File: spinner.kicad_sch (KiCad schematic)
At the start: 131 parts, among them J1 Micro_SD_Card, J301 USB_C_Receptacle_USB2.0_16P, J302 Conn_01x02_Pin, SW1 SW_SPDT, U2 RS0102, U301 BQ24073RGT, U302 SPX3819M5-L-3-3, U303 TPS61022, u10 ESP32-S3-WROOM-1

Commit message: Added a few more pinouts to the CPU.
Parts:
- added C301: 1uF, Capacitor_SMD:C_0805_2012Metric_Pad1.18x1.45mm_HandSolder, symbol Device:C
- added R310: 5.1k, Resistor_SMD:R_0603_1608Metric, symbol Device:R
- added SW301, SW302: SW_MEC_5E, symbol Switch:SW_MEC_5E
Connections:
- net +3V3: now also u10.2 (3V3), R310.1
- net DI: no longer D0.6 (DO), D101.1 (DI)
- net GND: now also u10.1 (GND), u10.40 (GND), u10.41 (GND), SW301.2, SW302.3 (K)
- net at u10.27 (GPIO0/BOOT): now also SW302.1
- net at u10.3 (EN): now also C301.2
- net CHG_L: no longer names the net of D325.1 (K), U301.9 (~{CHG})
- net PGOOD_L: no longer names the net of D326.1 (K), U301.7 (~{PGOOD})
- new net: C301.1, R310.2, SW301.4 (A)
- new net: D0.6 (DO), D101.1 (DI)
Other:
- note added: "DO NOT USE 28 - 30"

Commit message: More pinout choices, random dart throwing. Will test.
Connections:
- net OPTO_in_0: now also u10.32 (MTCK/GPIO39/CLK_OUT3/SUBSPICS1)
- net OPTO_in_1: now also u10.33 (MTDO/GPIO40/CLK_OUT2)
- net OPTO_in_2: now also u10.34 (MTDI/GPIO41/CLK_OUT1)
- net cmd: now also u10.18 (GPIO10/TOUCH10/ADC1_CH9/FSPICS0/FSPIIO4/SUBSPICS0)
- net dat_0: now also u10.19 (GPIO11/TOUCH11/ADC2_CH0/FSPID/FSPIIO5/SUBSPID)
- net dat_1: now also u10.20 (GPIO12/TOUCH12/ADC2_CH1/FSPICLK/FSPIIO6/SUBSPICLK)
- net dat_2: now also u10.21 (GPIO13/TOUCH13/ADC2_CH2/FSPIQ/FSPIIO7/SUBSPIQ)
- net dat_3: now also u10.22 (GPIO14/TOUCH14/ADC2_CH3/FSPIWP/FSPIDQS/SUBSPIWP)
- net spi_clk: now also u10.17 (GPIO9/TOUCH9/ADC1_CH8/FSPIHD/SUBSPIHD)
- net CI_3v3: now reaches U2.6 (A2)
- net CI_3v3: now also u10.11 (GPIO18/U1RXD/ADC2_CH7/CLK_OUT3)
- net DI_3v3: now reaches U2.7 (A1)
- net DI_3v3: now also u10.10 (GPIO17/U1TXD/ADC2_CH6)
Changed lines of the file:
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@@
+	(wire
+		(pts
+			(xy 815.34 111.76) (xy 829.31 111.76)
+		)
+		(stroke
+			(width 0)
+			(type default)
+		)
+	)
 	(wire
 		(pts
@@
 	(wire
 		(pts
+			(xy 815.34 104.14) (xy 829.31 104.14)
+		)
+		(stroke
+			(width 0)
+			(type default)
+		)
+	)
+	(wire
+		(pts
 			(xy 78.74 285.75) (xy 78.74 288.29)
 		)
@@
 	(wire
 		(pts
+			(xy 717.55 83.82) (xy 723.9 83.82)
+		)
+		(stroke
+			(width 0)
+			(type default)
+		)
+	)
+	(wire
+		(pts
 			(xy 180.34 68.58) (xy 181.61 68.58)
 		)
@@
 	(wire
 		(pts
+			(xy 815.34 119.38) (xy 829.31 119.38)
+		)
+		(stroke
+			(width 0)
+			(type default)
+		)
+	)
+	(wire
+		(pts
+			(xy 815.34 101.6) (xy 829.31 101.6)
+		)
+		(stroke
+			(width 0)
+			(type default)
+		)
+	)
+	(wire
+		(pts
 			(xy 66.04 256.54) (xy 78.74 256.54)
 		)
@@
 	(wire
 		(pts
+			(xy 815.34 116.84) (xy 829.31 116.84)
+		)
+		(stroke
+			(width 0)
+			(type default)
+		)
+	)
+	(wire
+		(pts
 			(xy 177.8 254) (xy 180.34 254)
 		)
@@
 	(wire
 		(pts
+			(xy 815.34 106.68) (xy 829.31 106.68)
+		)
+		(stroke
+			(width 0)
+			(type default)
+		)
+	)
+	(wire
+		(pts
 			(xy 600.71 261.62) (xy 604.52 261.62)
 		)
@@
 	(wire
 		(pts
+			(xy 717.55 81.28) (xy 723.9 81.28)
+		)
+		(stroke
+			(width 0)
+			(type default)
+		)
+	)
+	(wire
+		(pts
 			(xy 180.34 287.02) (xy 205.74 287.02)
 		)
@@
 	(wire
 		(pts
+			(xy 140.97 69.85) (xy 146.05 69.85)
+		)
+		(stroke
+			(width 0)
+			(type default)
+		)
+	)
+	(wire
+		(pts
 			(xy 646.43 261.62) (xy 638.81 261.62)
 		)
@@
 	(wire
 		(pts
+			(xy 815.34 114.3) (xy 829.31 114.3)
+		)
+		(stroke
+			(width 0)
+			(type default)
+		)
+	)
+	(wire
+		(pts
 			(xy 93.98 256.54) (xy 96.52 256.54)
 		)
@@
 	(wire
 		(pts
+			(xy 140.97 64.77) (xy 146.05 64.77)
+		)
+		(stroke
+			(width 0)
+			(type default)
+		)
+	)
+	(wire
+		(pts
 			(xy 175.26 276.86) (xy 205.74 276.86)
 		)
@@
 	(wire
 		(pts
+			(xy 815.34 109.22) (xy 829.31 109.22)
+		)
+		(stroke
+			(width 0)
+			(type default)
+		)
+	)
+	(wire
+		(pts
 			(xy 474.98 297.18) (xy 466.09 297.18)
 		)
@@
 		(pts
 			(xy 78.74 313.69) (xy 78.74 307.34)
+		)
+		(stroke
+			(width 0)
+			(type default)
+		)
+	)
+	(wire
+		(pts
+			(xy 717.55 78.74) (xy 723.9 78.74)
 		)
 		(stroke
@@
 		)
 	)
+	(label "dat_2"
+		(at 829.31 111.76 0)
+		(effects
+			(font
+				(size 1.27 1.27)
+			)
+			(justify left bottom)
+		)
+	)
+	(label "dat_3"
+		(at 829.31 114.3 0)
+		(effects
+			(font
+				(size 1.27 1.27)
+			)
+			(justify left bottom)
+		)
+	)
 	(label "DI"
 		(at 54.61 25.4 0)
@@
 		)
 	)
+	(label "spi_clk"
+		(at 829.31 101.6 0)
+		(effects
+			(font
+				(size 1.27 1.27)
+			)
+			(justify left bottom)
+		)
+	)
 	(label "DI"
 		(at 118.11 64.77 0)
@@
 		)
 	)
+	(label "DI_3v3"
+		(at 146.05 64.77 0)
+		(effects
+			(font
+				(size 1.27 1.27)
+			)
+			(justify left bottom)
+		)
+	)
+	(label "dat_0"
+		(at 829.31 106.68 0)
+		(effects
+			(font
+				(size 1.27 1.27)
+			)
+			(justify left bottom)
+		)
+	)
 	(label "DO_1"
 		(at 173.99 119.38 0)
@@
 		)
 	)
+	(label "cmd"
+		(at 829.31 104.14 0)
+		(effects
+			(font
+				(size 1.27 1.27)
+			)
+			(justify left bottom)
+		)
+	)
 	(label "dat_2"
 		(at 162.56 271.78 180)
@@
 		)
 	)
+	(label "DI_3v3"
+		(at 829.31 116.84 0)
+		(effects
+			(font
+				(size 1.27 1.27)
+			)
+			(justify left bottom)
+		)
+	)
 	(label "CI"
 		(at 118.11 69.85 0)
@@
 		)
 	)
+	(label "OPTO_in_0"
+		(at 717.55 78.74 180)
+		(effects
+			(font
+				(size 1.27 1.27)
+			)
+			(justify right bottom)
+		)
+	)
 	(label "CO_1"
 		(at 173.99 121.92 0)
@@
 		)
 	)
+	(label "OPTO_in_1"
+		(at 717.55 81.28 180)
+		(effects
+			(font
+				(size 1.27 1.27)
+			)
+			(justify right bottom)
+		)
+	)
 	(label "DI"
 		(at 158.75 66.04 0)
@@
 		)
 	)
+	(label "dat_1"
+		(at 829.31 109.22 0)
+		(effects
+			(font
+				(size 1.27 1.27)
+			)
+			(justify left bottom)
+		)
+	)
+	(label "OPTO_in_2"
+		(at 717.55 83.82 180)
+		(effects
+			(font
+				(size 1.27 1.27)
+			)
+			(justify right bottom)
+		)
+	)
 	(label "dat_3"
 		(at 162.56 274.32 180)
@@
 		)
 	)
+	(label "CI_3v3"
+		(at 829.31 119.38 0)
+		(effects
+			(font
+				(size 1.27 1.27)
+			)
+			(justify left bottom)
+		)
+	)
 	(label "CI"
 		(at 158.75 68.58 0)
 		(effects
 			(font
+				(size 1.27 1.27)
+			)
+			(justify left bottom)
+		)
+	)
+	(label "CI_3v3"
+		(at 146.05 69.85 0)
+		(effects
+			(font

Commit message: Added touch pads.
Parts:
- added R311, R312, R313, R314, R315, R316, R317, R318: 510, Resistor_SMD:R_0603_1608Metric, symbol Device:R
- added TP301, TP302, TP303, TP304, TP305, TP306, TP307, TP308: TestPoint, symbol Connector:TestPoint
- D325, D326: footprint (none) -> LED_SMD:LED_0805_2012Metric
- TP4: value VCC -> 5VCC
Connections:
- net VCC is gone; now on net +5V: D0.4 (VCC), D101.4 (VCC), D102.4 (VCC), D103.4 (VCC), D104.4 (VCC), D105.4 (VCC), D106.4 (VCC), D107.4 (VCC), D108.4 (VCC), D109.4 (VCC), D110.4 (VCC), D111.4 (VCC), D112.4 (VCC), D113.4 (VCC), D114.4 (VCC), D115.4 (VCC), D116.4 (VCC), D117.4 (VCC), D118.4 (VCC), D119.4 (VCC), D120.4 (VCC), D121.4 (VCC), D122.4 (VCC), D123.4 (VCC), D124.4 (VCC), D201.4 (VCC), D202.4 (VCC), D203.4 (VCC), D204.4 (VCC), D205.4 (VCC), D206.4 (VCC), D207.4 (VCC), D208.4 (VCC), D209.4 (VCC), D210.4 (VCC), D211.4 (VCC), D212.4 (VCC), D213.4 (VCC), D214.4 (VCC), D215.4 (VCC), D216.4 (VCC), D217.4 (VCC), D218.4 (VCC), D219.4 (VCC), D220.4 (VCC), D221.4 (VCC), D222.4 (VCC), D223.4 (VCC), D224.4 (VCC), D301.4 (VCC), D302.4 (VCC), D303.4 (VCC), D304.4 (VCC), D305.4 (VCC), D306.4 (VCC), D307.4 (VCC), D308.4 (VCC), D309.4 (VCC), D310.4 (VCC), D311.4 (VCC), D312.4 (VCC), D313.4 (VCC), D314.4 (VCC), D315.4 (VCC), D316.4 (VCC), D317.4 (VCC), D318.4 (VCC), D319.4 (VCC), D320.4 (VCC), D321.4 (VCC), D322.4 (VCC), D323.4 (VCC), D324.4 (VCC), D327.2 (A), D328.2 (A), D329.2 (A), TP4.1, U2.1 (VCCB)
- net touch_pad_08: now reaches u10.12 (GPIO8/TOUCH8/ADC1_CH7/SUBSPICS1)
- net touch_pad_08: now also R318.1
- net touch_pad_03: now reaches u10.15 (GPIO3/TOUCH3/ADC1_CH2)
- net touch_pad_03: now also R313.1
- net touch_pad_02: now reaches u10.38 (GPIO2/TOUCH2/ADC1_CH1)
- net touch_pad_02: now also R312.1
- net touch_pad_01: now reaches u10.39 (GPIO1/TOUCH1/ADC1_CH0)
- net touch_pad_01: now also R311.1
- net touch_pad_04: now reaches u10.4 (GPIO4/TOUCH4/ADC1_CH3)
- net touch_pad_04: now also R314.1
- net touch_pad_05: now reaches u10.5 (GPIO5/TOUCH5/ADC1_CH4)
- net touch_pad_05: now also R315.1
- net touch_pad_06: now reaches u10.6 (GPIO6/TOUCH6/ADC1_CH5)
- net touch_pad_06: now also R316.1
- net touch_pad_07: now reaches u10.7 (GPIO7/TOUCH7/ADC1_CH6)
- net touch_pad_07: now also R317.1
- new net: R311.2, TP301.1
- new net: R316.2, TP306.1
- new net: R317.2, TP307.1
- new net: R312.2, TP302.1
- new net: R313.2, TP303.1
- new net: R314.2, TP304.1
- new net: R318.2, TP308.1
- new net: R315.2, TP305.1
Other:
- note added: "Test Points"
- note added: "Touch Pads"
- moved on the sheet: TP1, TP5, TP6, TP7, TP8, TP9

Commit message: Adding recent work.  schematic & layout are done-ish
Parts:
- removed R316, R317, R318: 510, Resistor_SMD:R_0603_1608Metric, symbol Device:R
- removed SW301, SW302: SW_MEC_5E, symbol Switch:SW_MEC_5E
- removed TP301, TP302, TP303, TP304, TP305, TP306, TP307, TP308: TestPoint, symbol Connector:TestPoint
- added SW301: RESET, Button_Switch_SMD:SW_Push_SPST_NO_Alps_SKRK, symbol Switch:SW_Push
- added SW302: BOOT, Button_Switch_SMD:SW_Push_SPST_NO_Alps_SKRK, symbol Switch:SW_Push
- added TP309: TestPoint_2Pole, Library:TouchSlider-2_20x10mm, symbol Connector:TestPoint_2Pole
- R1, R2, R3: value ~3.3k -> 3.3k
- R313, R314, R315: value 510 -> 1k
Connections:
- net +3V3: now also R313.2; no longer TP3.1
- net +5V: now also R314.2; no longer TP4.1
- net +BATT: now also R315.2; no longer TP9.1
- net GND: now also SW301.1, SW302.2
- net at C301.1, R310.2: now also SW301.2
- net at R311.2: now also TP309.1
- net at u10.27 (GPIO0/BOOT): now also SW302.1
- net at R312.2: now also TP309.2
- net touch_pad_03: no longer names the net of u10.15 (GPIO3/TOUCH3/ADC1_CH2)
- net touch_pad_03: no longer R313.1
- net touch_pad_04: no longer names the net of R314.1
- net touch_pad_04: now also TP4.1; no longer u10.4 (GPIO4/TOUCH4/ADC1_CH3)
- net touch_pad_05: no longer names the net of R315.1
- net touch_pad_05: now also TP9.1; no longer u10.5 (GPIO5/TOUCH5/ADC1_CH4)
- net touch_pad_06: no longer names the net of u10.6 (GPIO6/TOUCH6/ADC1_CH5)
- net touch_pad_07: no longer names the net of u10.7 (GPIO7/TOUCH7/ADC1_CH6)
- net touch_pad_08: no longer names the net of u10.12 (GPIO8/TOUCH8/ADC1_CH7/SUBSPICS1)
- new net: R313.1, TP3.1
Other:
- moved on the sheet: TP1, TP2, TP3, TP4, TP5, TP6, TP7, TP8, TP9

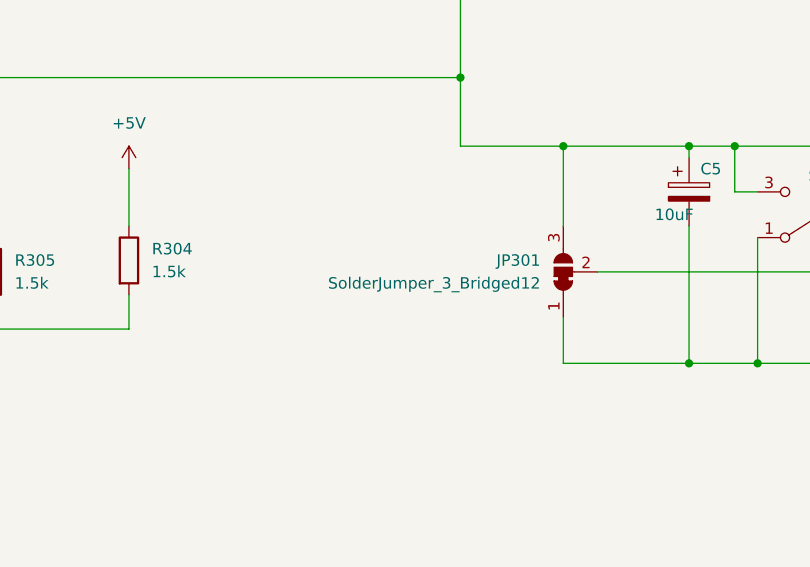
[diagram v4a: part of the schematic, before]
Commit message: Do some layout things. Hey remember to add footprints.
Some parts aren't on the layout cause schematic parts
don't have footprints.
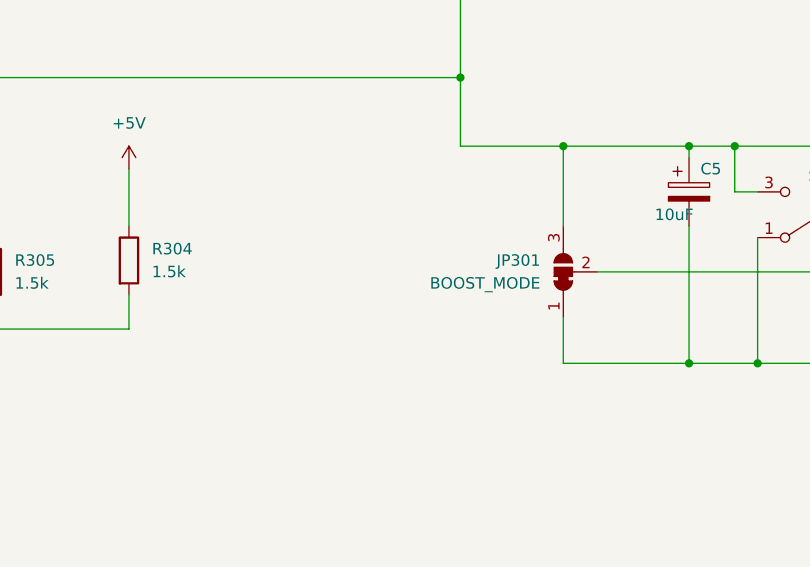
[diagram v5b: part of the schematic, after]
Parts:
- JP301: value SolderJumper_3_Bridged12 -> BOOST_MODE
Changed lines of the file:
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@@
 			)
 		)
-		(property "Value" "SolderJumper_3_Bridged12"
+		(property "Value" "BOOST_MODE"
 			(at 566.42 269.2399 90)
 			(effects

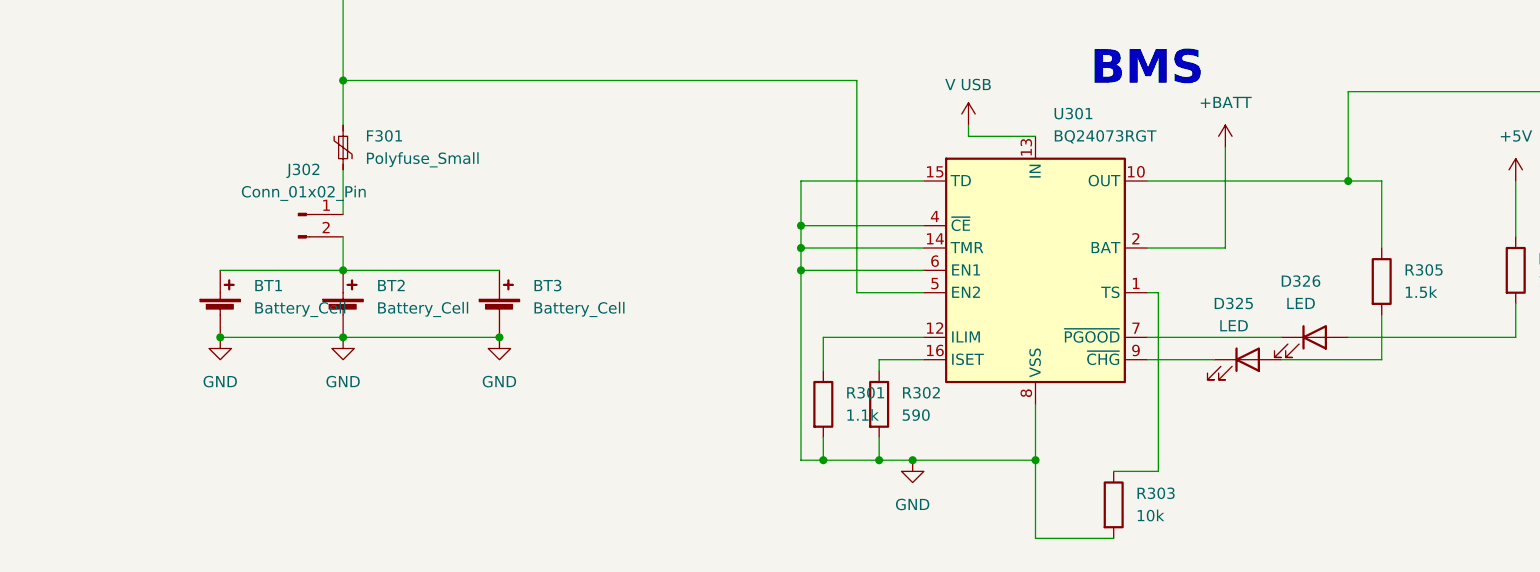
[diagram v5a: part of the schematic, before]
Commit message: Added footprint for SMD pin header.  and layout things.
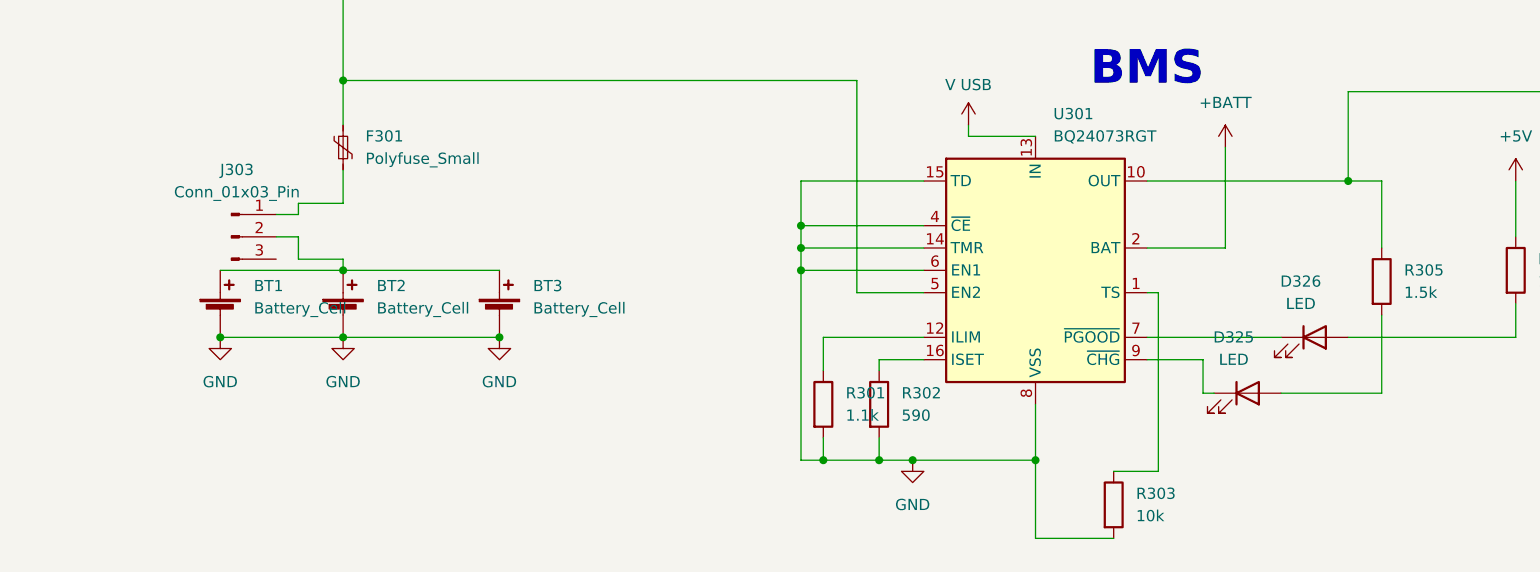
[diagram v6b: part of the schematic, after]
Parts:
- removed J302: Conn_01x02_Pin, symbol Connector:Conn_01x02_Pin
- added J303: Conn_01x03_Pin, Connector_PinHeader_1.00mm:PinHeader_1x03_P1.00mm_Vertical, symbol Connector:Conn_01x03_Pin
- F301: footprint (none) -> Resistor_SMD:R_1210_3225Metric
- R301, R302, R303, R304, R305: footprint (none) -> Resistor_SMD:R_0805_2012Metric_Pad1.20x1.40mm_HandSolder
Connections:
- net at F301.2: now also J303.1 (Pin_1)
- net at BT1.1 (+), BT2.1 (+), BT3.1 (+): now also J303.2 (Pin_2)
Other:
- moved on the sheet: D325
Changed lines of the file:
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@@
 	(wire
 		(pts
-			(xy 505.46 276.86) (xy 494.03 276.86)
-		)
-		(stroke
-			(width 0)
-			(type default)
-		)
-	)
-	(wire
-		(pts
 			(xy 501.65 246.38) (xy 501.65 256.54)
 		)
@@
 	(wire
 		(pts
-			(xy 505.46 271.78) (xy 505.46 276.86)
+			(xy 300.99 121.92) (xy 302.26 121.92)
 		)
 		(stroke
@@
 	(wire
 		(pts
-			(xy 300.99 121.92) (xy 302.26 121.92)
+			(xy 815.34 78.74) (xy 834.39 78.74)
 		)
 		(stroke
@@
 	(wire
 		(pts
-			(xy 815.34 78.74) (xy 834.39 78.74)
+			(xy 638.81 236.22) (xy 638.81 254)
 		)
 		(stroke
@@
 	(wire
 		(pts
-			(xy 638.81 236.22) (xy 638.81 254)
+			(xy 453.39 276.86) (xy 448.31 276.86)
 		)
 		(stroke
@@
 	(wire
 		(pts
-			(xy 453.39 276.86) (xy 448.31 276.86)
+			(xy 505.46 280.67) (xy 505.46 271.78)
 		)
 		(stroke
@@
 	(wire
 		(pts
+			(xy 382.27 259.08) (xy 387.35 259.08)
+		)
+		(stroke
+			(width 0)
+			(type default)
+		)
+	)
+	(wire
+		(pts
 			(xy 170.18 254) (xy 170.18 251.46)
 		)
@@
 	(wire
 		(pts
+			(xy 379.73 260.35) (xy 382.27 260.35)
+		)
+		(stroke
+			(width 0)
+			(type default)
+		)
+	)
+	(wire
+		(pts
 			(xy 466.09 281.94) (xy 466.09 288.29)
 		)
@@
 	(wire
 		(pts
-			(xy 387.35 262.89) (xy 387.35 266.7)
+			(xy 382.27 262.89) (xy 382.27 265.43)
 		)
 		(stroke
@@
 	(wire
 		(pts
+			(xy 387.35 265.43) (xy 387.35 266.7)
+		)
+		(stroke
+			(width 0)
+			(type default)
+		)
+	)
+	(wire
+		(pts
 			(xy 702.31 53.34) (xy 715.01 53.34)
 		)
@@
 	(wire
 		(pts
-			(xy 387.35 255.27) (xy 387.35 260.35)
+			(xy 382.27 259.08) (xy 382.27 260.35)
 		)
 		(stroke
@@
 	(wire
 		(pts
+			(xy 485.14 280.67) (xy 485.14 276.86)
+		)
+		(stroke
+			(width 0)
+			(type default)
+		)
+	)
+	(wire
+		(pts
 			(xy 118.11 64.77) (xy 120.65 64.77)
 		)
@@
 	(wire
 		(pts
-			(xy 478.79 276.86) (xy 486.41 276.86)
+			(xy 382.27 265.43) (xy 387.35 265.43)
+		)
+		(stroke
+			(width 0)
+			(type default)
+		)
+	)
+	(wire
+		(pts
+			(xy 485.14 280.67) (xy 486.41 280.67)
 		)
 		(stroke
@@
 	(wire
 		(pts
+			(xy 485.14 276.86) (xy 478.79 276.86)
+		)
+		(stroke
+			(width 0)
+			(type default)
+		)
+	)
+	(wire
+		(pts
 			(xy 480.06 269.24) (xy 480.06 289.56)
 		)
@@
 	(wire
 		(pts
+			(xy 379.73 262.89) (xy 382.27 262.89)
+		)
+		(stroke
+			(width 0)
+			(type default)
+		)
+	)
+	(wire
+		(pts
 			(xy 505.46 256.54) (xy 501.65 256.54)
 		)
@@
 	(wire
 		(pts
+			(xy 387.35 259.08) (xy 387.35 255.27)
+		)
+		(stroke
+			(width 0)
+			(type default)
+		)
+	)
+	(wire
+		(pts
 			(xy 309.88 267.97) (xy 323.85 267.97)
 		)
@@
 	(wire
 		(pts
+			(xy 494.03 280.67) (xy 505.46 280.67)
+		)
+		(stroke
+			(width 0)
+			(type default)
+		)
+	)
+	(wire
+		(pts
 			(xy 453.39 256.54) (xy 439.42 256.54)
 		)
@@
 			)
 		)
-		(property "Footprint" ""
+		(property "Footprint" "Resistor_SMD:R_0805_2012Metric_Pad1.20x1.40mm_HandSolder"
 			(at 518.922 266.7 90)
 			(effects
@@
 			)
 		)
-		(property "Footprint" ""
+		(property "Footprint" "Resistor_SMD:R_1210_3225Metric"
 			(at 388.62 257.81 0)
 			(effects
@@
 			)
 		)
-		(property "Footprint" ""
+		(property "Footprint" "Resistor_SMD:R_0805_2012Metric_Pad1.20x1.40mm_HandSolder"
 			(at 446.532 281.94 90)
 			(effects
@@
 			)
 		)
-		(property "Footprint" ""
+		(property "Footprint" "Resistor_SMD:R_0805_2012Metric_Pad1.20x1.40mm_HandSolder"
 			(at 440.182 281.94 90)
 			(effects
@@
 	)
 	(symbol
-		(lib_id "Connector:Conn_01x02_Pin")
-		(at 382.27 260.35 0)
-		(unit 1)
-		(exclude_from_sim no)
-		(in_bom yes)
-		(on_board yes)
-		(dnp no)
-		(fields_autoplaced yes)
-		(property "Reference" "J302"
-			(at 382.905 255.27 0)
-			(effects
-				(font
-					(size 1.27 1.27)
-				)
-			)
-		)
-		(property "Value" "Conn_01x02_Pin"
-			(at 382.905 257.81 0)
-			(effects
-				(font
-					(size 1.27 1.27)
-				)
-			)
-		)
-		(property "Footprint" ""
-			(at 382.27 260.35 0)
-			(effects
-				(font
-					(size 1.27 1.27)
-				)
-				(hide yes)
-			)
-		)
-		(property "Datasheet" "~"
-			(at 382.27 260.35 0)
-			(effects
-				(font
-					(size 1.27 1.27)
-				)
-				(hide yes)
-			)
-		)
-		(property "Description" "Generic connector, single row, 01x02, script generated"
-			(at 382.27 260.35 0)
-			(effects
-				(font
-					(size 1.27 1.27)
-				)
-				(hide yes)
-			)
-		)
-		(pin "1"
-		)
-		(pin "2"
-		)
-		(instances
-			(project ""
-				(path "/05674d5f-20d4-4623-8618-aef1dce549a6"
-					(reference "J302")
-					(unit 1)
-				)
-			)
-		)
-	)
-	(symbol
 		(lib_id "LED:APA102")
 		(at 360.68 68.58 0)
@@
 			)
 		)
-		(property "Footprint" ""
+		(property "Footprint" "Resistor_SMD:R_0805_2012Metric_Pad1.20x1.40mm_HandSolder"
 			(at 503.682 267.97 90)
 			(effects
@@
 			)
 		)
-		(property "Footprint" ""
+		(property "Footprint" "Resistor_SMD:R_0805_2012Metric_Pad1.20x1.40mm_HandSolder"
 			(at 473.202 293.37 90)
 			(effects
@@
 	)
 	(symbol
+		(lib_id "Connector:Conn_01x03_Pin")
+		(at 374.65 262.89 0)
+		(unit 1)
+		(exclude_from_sim no)
+		(in_bom yes)
+		(on_board yes)
+		(dnp no)
+		(fields_autoplaced yes)
+		(property "Reference" "J303"
+			(at 375.285 255.27 0)
+			(effects
+				(font
+					(size 1.27 1.27)
+				)
+			)
+		)
+		(property "Value" "Conn_01x03_Pin"
+			(at 375.285 257.81 0)
+			(effects
+				(font
+					(size 1.27 1.27)
+				)
+			)
+		)
+		(property "Footprint" "Connector_PinHeader_1.00mm:PinHeader_1x03_P1.00mm_Vertical"
+			(at 374.65 262.89 0)
+			(effects
+				(font
+					(size 1.27 1.27)
+				)
+				(hide yes)
+			)
+		)
+		(property "Datasheet" "~"
+			(at 374.65 262.89 0)
+			(effects
+				(font
+					(size 1.27 1.27)
+				)
+				(hide yes)
+			)
+		)
+		(property "Description" "Generic connector, single row, 01x03, script generated"
+			(at 374.65 262.89 0)
+			(effects
+				(font
+					(size 1.27 1.27)
+				)
+				(hide yes)
+			)
+		)
+		(pin "1"
+		)
+		(pin "3"
+		)
+		(pin "2"
+		)
+		(instances
+			(project ""
+				(path "/05674d5f-20d4-4623-8618-aef1dce549a6"
+					(reference "J303")
+					(unit 1)
+				)
+			)
+		)
+	)
+	(symbol
 		(lib_id "power:GND")
 		(at 217.17 129.54 0)
@@
 	(symbol
 		(lib_id "Device:LED")
-		(at 490.22 276.86 0)
+		(at 490.22 280.67 0)
 		(unit 1)
 		(exclude_from_sim no)
@@
 		(fields_autoplaced yes)
 		(property "Reference" "D325"
-			(at 488.6325 270.51 0)
+			(at 488.6325 274.32 0)
 			(effects
 				(font
@@
 		)
 		(property "Value" "LED"
-			(at 488.6325 273.05 0)
+			(at 488.6325 276.86 0)
 			(effects
 				(font
@@
 		)
 		(property "Footprint" "LED_SMD:LED_0805_2012Metric"
-			(at 490.22 276.86 0)
+			(at 490.22 280.67 0)
 			(effects
 				(font
@@
 		)
 		(property "Datasheet" "~"
-			(at 490.22 276.86 0)
+			(at 490.22 280.67 0)
 			(effects
 				(font
@@
 		)
 		(property "Description" ""
-			(at 490.22 276.86 0)
+			(at 490.22 280.67 0)
 			(effects
 				(font
